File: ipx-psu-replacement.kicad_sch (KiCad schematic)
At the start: 31 parts, among them J1 L, J10 -12V, J11 GND, J12 Fan, J13 SENS, J14 GND, J15 GND, J2 AC IN, J3 GND, J4 Floppy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

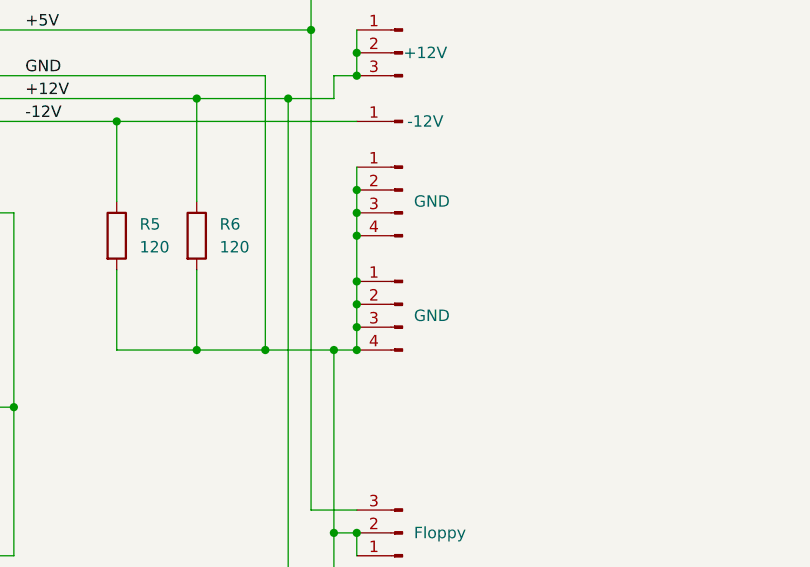
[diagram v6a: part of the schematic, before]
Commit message: correct mounting hole locations
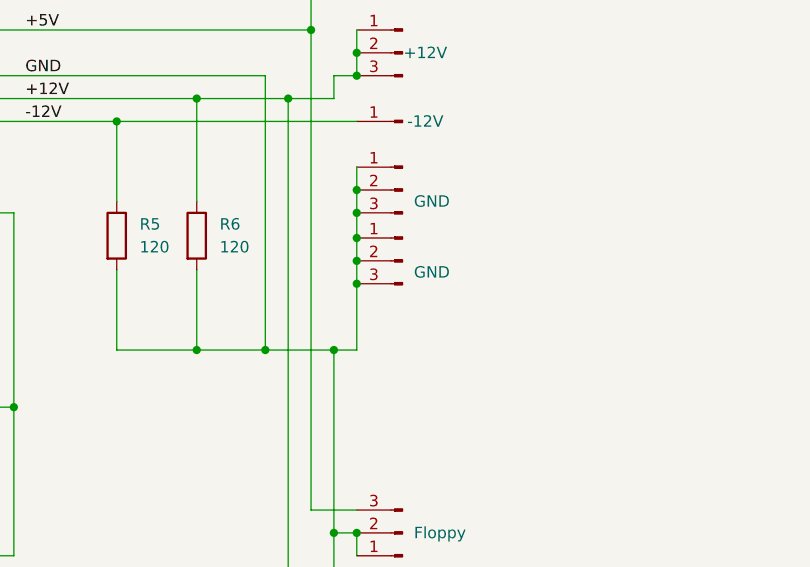
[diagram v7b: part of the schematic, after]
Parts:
- J11, J3: footprint Connector_Wire:SolderWire-1.5sqmm_1x04_P6mm_D1.7mm_OD3mm -> Connector_Wire:SolderWire-1.5sqmm_1x03_P6mm_D1.7mm_OD3mm; symbol Connector:Conn_01x04_Pin -> Connector:Conn_01x03_Pin
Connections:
- net GND: no longer J11.4 (Pin_4), J3.4 (Pin_4)
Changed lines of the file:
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@@
   (junction (at 81.026 40.386) (diameter 0) (color 0 0 0 0)
   )
-  (junction (at 194.31 118.11) (diameter 0) (color 0 0 0 0)
-  )
   (junction (at 189.23 82.55) (diameter 0) (color 0 0 0 0)
   )
   (junction (at 155.194 62.484) (diameter 0) (color 0 0 0 0)
   )
-  (junction (at 194.31 113.03) (diameter 0) (color 0 0 0 0)
-  )
   (junction (at 194.31 87.63) (diameter 0) (color 0 0 0 0)
   )
@@
   (junction (at 186.69 90.17) (diameter 0) (color 0 0 0 0)
   )
-  (junction (at 194.31 105.41) (diameter 0) (color 0 0 0 0)
-  )
   (junction (at 173.736 35.052) (diameter 0) (color 0 0 0 0)
   )
@@
   (junction (at 194.31 85.09) (diameter 0) (color 0 0 0 0)
   )
-  (junction (at 194.31 115.57) (diameter 0) (color 0 0 0 0)
-  )
   (junction (at 184.15 118.11) (diameter 0) (color 0 0 0 0)
   )
@@
   (junction (at 55.626 27.94) (diameter 0) (color 0 0 0 0)
   )
+  (junction (at 194.31 105.664) (diameter 0) (color 0 0 0 0)
+  )
   (junction (at 128.27 102.87) (diameter 0) (color 0 0 0 0)
   )
   (junction (at 176.53 118.11) (diameter 0) (color 0 0 0 0)
   )
+  (junction (at 194.31 108.204) (diameter 0) (color 0 0 0 0)
+  )
   (junction (at 191.77 138.43) (diameter 0) (color 0 0 0 0)
   )
@@
   (junction (at 194.31 100.33) (diameter 0) (color 0 0 0 0)
   )
-  (junction (at 194.31 110.49) (diameter 0) (color 0 0 0 0)
-  )
   (junction (at 62.23 102.87) (diameter 0) (color 0 0 0 0)
   )
@@
   )
   (junction (at 133.35 124.46) (diameter 0) (color 0 0 0 0)
+  )
+  (junction (at 194.31 110.744) (diameter 0) (color 0 0 0 0)
   )
   (no_connect (at 152.4 153.67))
@@
     (stroke (width 0) (type default))
   )
-  (wire (pts (xy 194.31 115.57) (xy 194.31 118.11))
+  (wire (pts (xy 194.31 108.204) (xy 194.31 110.744))
     (stroke (width 0) (type default))
   )
@@
     (stroke (width 0) (type default))
   )
-  (wire (pts (xy 194.31 113.03) (xy 194.31 115.57))
-    (stroke (width 0) (type default))
-  )
   (wire (pts (xy 194.31 72.39) (xy 194.31 74.93))
     (stroke (width 0) (type default))
@@
     (stroke (width 0) (type default))
   )
+  (wire (pts (xy 194.31 110.744) (xy 194.31 118.11))
+    (stroke (width 0) (type default))
+  )
   (wire (pts (xy 141.478 55.372) (xy 173.736 55.372))
     (stroke (width 0) (type default))
@@
     (stroke (width 0) (type default))
   )
-  (wire (pts (xy 194.31 105.41) (xy 194.31 110.49))
+  (wire (pts (xy 194.31 102.87) (xy 194.31 105.664))
     (stroke (width 0) (type default))
   )
@@
     (stroke (width 0) (type default))
   )
-  (wire (pts (xy 194.31 102.87) (xy 194.31 105.41))
-    (stroke (width 0) (type default))
-  )
   (wire (pts (xy 184.15 118.11) (xy 191.77 118.11))
     (stroke (width 0) (type default))
@@
     (stroke (width 0) (type default))
   )
-  (wire (pts (xy 194.31 110.49) (xy 194.31 113.03))
-    (stroke (width 0) (type default))
-  )
   (wire (pts (xy 170.434 40.132) (xy 181.102 40.132))
     (stroke (width 0) (type default))
@@
   )
   (wire (pts (xy 156.21 102.87) (xy 156.21 124.46))
+    (stroke (width 0) (type default))
+  )
+  (wire (pts (xy 194.31 105.664) (xy 194.31 108.204))
     (stroke (width 0) (type default))
   )
@@
     )
   )
-  (symbol (lib_id "Connector:Conn_01x04_Pin") (at 199.39 113.03 0) (mirror y) (unit 1)
-    (in_bom yes) (on_board yes) (dnp no)
-    (property "Reference" "J11" (at 201.93 114.3 90)
-      (effects (font (size 1.27 1.27)) hide)
-    )
-    (property "Value" "GND" (at 200.66 114.3 0)
+  (symbol (lib_id "Connector:Conn_01x03_Pin") (at 199.39 108.204 0) (mirror y) (unit 1)
+    (in_bom yes) (on_board yes) (dnp no)
+    (property "Reference" "J11" (at 201.93 109.474 90)
+      (effects (font (size 1.27 1.27)) hide)
+    )
+    (property "Value" "GND" (at 200.66 109.474 0)
       (effects (font (size 1.27 1.27)) (justify right))
     )
-    (property "Footprint" "Connector_Wire:SolderWire-1.5sqmm_1x04_P6mm_D1.7mm_OD3mm" (at 199.39 113.03 0)
-      (effects (font (size 1.27 1.27)) hide)
-    )
-    (property "Datasheet" "~" (at 199.39 113.03 0)
+    (property "Footprint" "Connector_Wire:SolderWire-1.5sqmm_1x03_P6mm_D1.7mm_OD3mm" (at 199.39 108.204 0)
+      (effects (font (size 1.27 1.27)) hide)
+    )
+    (property "Datasheet" "~" (at 199.39 108.204 0)
       (effects (font (size 1.27 1.27)) hide)
     )
@@
     (pin "2")
     (pin "3")
-    (pin "4")
     (instances
       (project "ipx-psu-replacement"
@@
     )
   )
-  (symbol (lib_id "Connector:Conn_01x04_Pin") (at 199.39 100.33 0) (mirror y) (unit 1)
+  (symbol (lib_id "Connector:Conn_01x03_Pin") (at 199.39 100.33 0) (mirror y) (unit 1)
     (in_bom yes) (on_board yes) (dnp no)
     (property "Reference" "J3" (at 201.93 101.6 90)
@@
       (effects (font (size 1.27 1.27)) (justify right))
     )
-    (property "Footprint" "Connector_Wire:SolderWire-1.5sqmm_1x04_P6mm_D1.7mm_OD3mm" (at 199.39 100.33 0)
+    (property "Footprint" "Connector_Wire:SolderWire-1.5sqmm_1x03_P6mm_D1.7mm_OD3mm" (at 199.39 100.33 0)
       (effects (font (size 1.27 1.27)) hide)
     )
@@
     (pin "2")
     (pin "3")
-    (pin "4")
-    (instances
-      (project "ipx-psu-replacement"
+    (instances
+      (project "ipx-psu-replacement"
